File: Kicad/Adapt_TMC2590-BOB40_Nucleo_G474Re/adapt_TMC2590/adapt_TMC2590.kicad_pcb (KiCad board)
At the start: 2 copper layers, 56.5 x 56.7 mm, 14 parts, among them J1 Conn_01x02, J2 Conn_01x04, J3 Conn_01x06, J4 Conn_01x04, U1 NUCLEO-G474RE_ArduinoConn, U2 TMC2590-BOB40

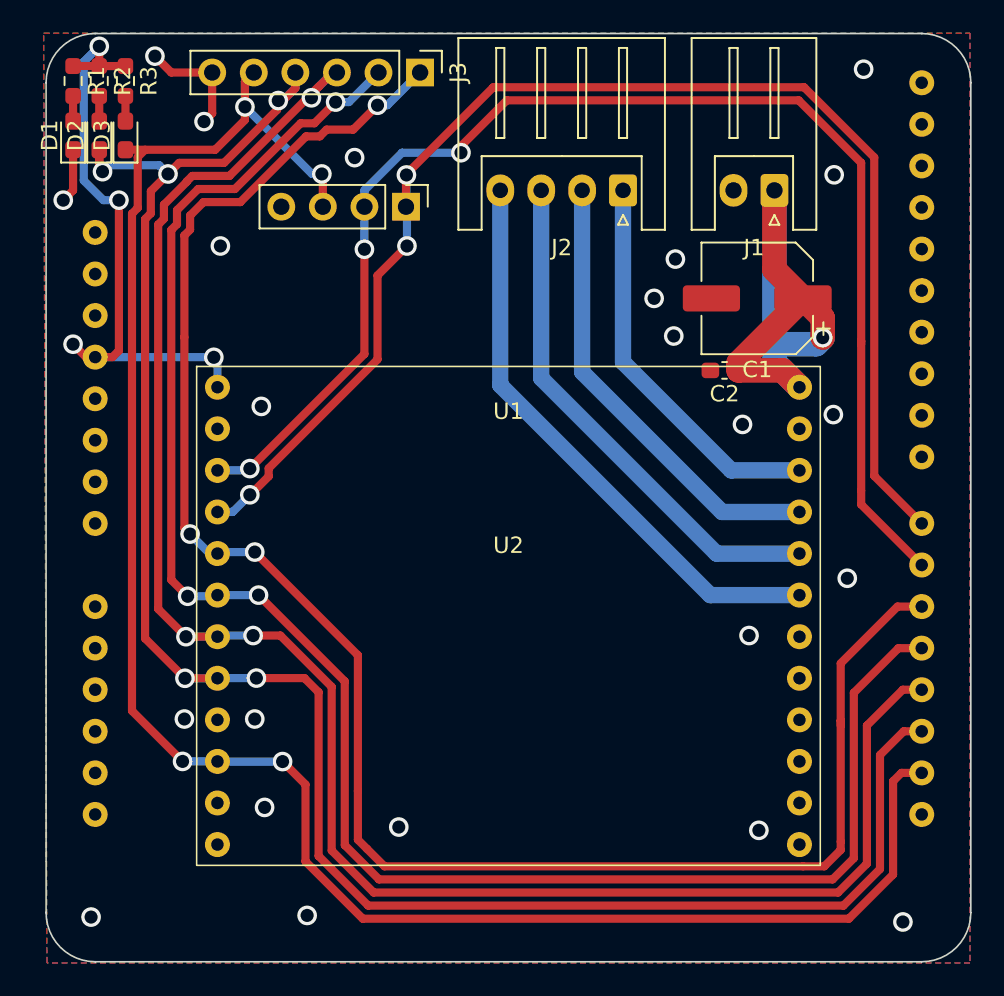
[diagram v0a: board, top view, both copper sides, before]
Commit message: create project for testing TMC2590 on NUCLEO-G474RET6
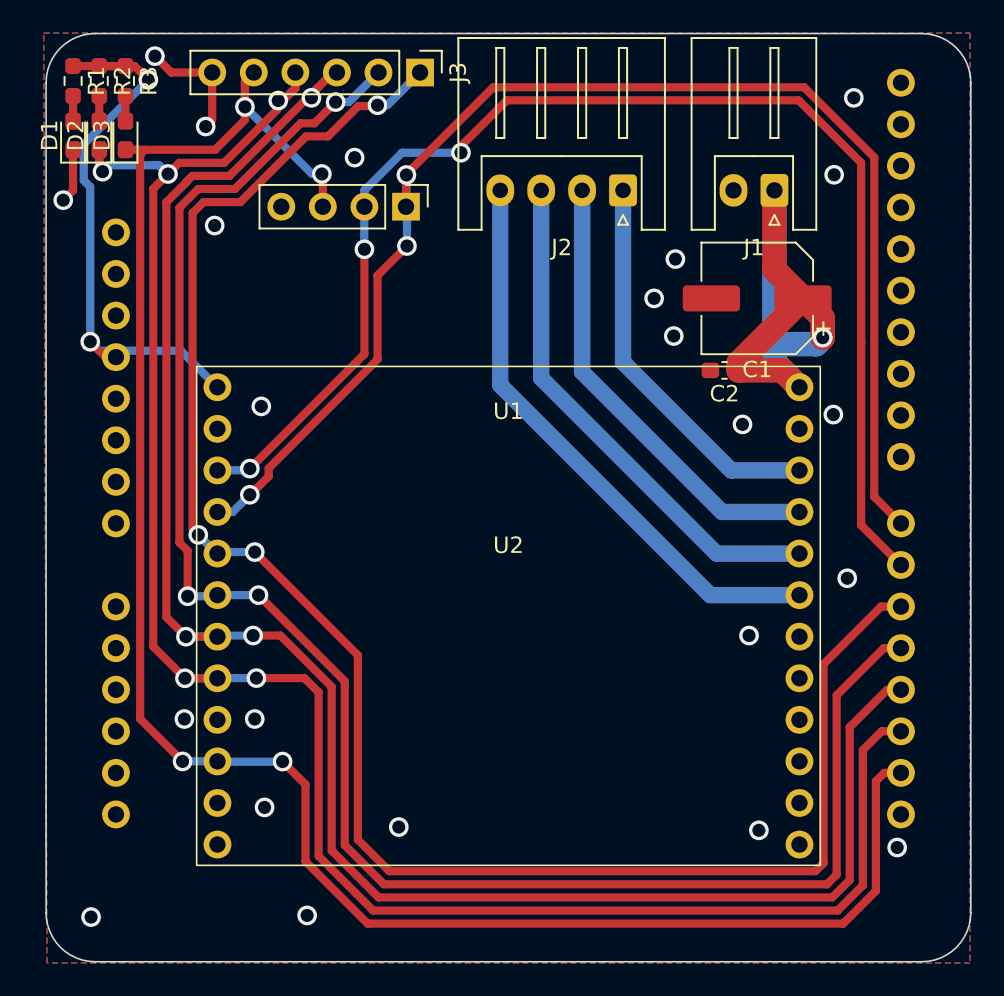
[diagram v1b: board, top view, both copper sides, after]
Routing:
- net +3.3V: track 37.3 -> 35.2 mm, vias 4 -> 2
- net /SPI3_MISO: track 110.8 -> 109.2 mm
- net /SPI3_MOSI: track 109.7 -> 108.7 mm
- net /SPI3_SCK: track 113.8 -> 112.9 mm
- net /DRV_ENN: track 119.8 -> 119.0 mm
- net /CSN: track 121.2 -> 120.5 mm
- net /TIM1_STEP: track 84.1 -> 83.6 mm
- net /DIR: track 82.7 -> 82.1 mm
